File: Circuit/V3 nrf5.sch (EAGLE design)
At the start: 77 parts, among them J4 USB Micro, J7 CORTEX_DEBUG_SMD, Q1 BSS138, Q2 BSS84, U1 AL8805, U2 MCP73831, U3 BC840M, U4 3.3V/150mA, U5 AL8805, U6 AL8805, U8 TPS61235PRWLR, Y1 32.768kHz

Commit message: clean brd
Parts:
- D2: DIGIKEY 160-1837-1-ND -> (none)
- D9: DIGIKEY 160-1436-1-ND -> (none)
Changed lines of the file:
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@@
 <part name="GND1" library="SparkFun-PowerSymbols" deviceset="GND" device=""/>
 <part name="GND20" library="SparkFun-PowerSymbols" deviceset="GND" device=""/>
-<part name="D2" library="SparkFun-LED" library_urn="urn:adsk.eagle:library:529" deviceset="LED-BLUE" device="0603" package3d_urn="urn:adsk.eagle:package:39354/1" value="BLUE">
-<attribute name="DIGIKEY" value="160-1837-1-ND"/>
-</part>
 <part name="R5" library="SparkFun-Resistors" deviceset="1KOHM" device="-0603-1/10W-1%" value="1k">
 <attribute name="DIGIKEY" value="RMCF0603FG1K00"/>
@@
 <part name="D8" library="SparkFun-DiscreteSemi" deviceset="DIODE-SCHOTTKY" device="-B340A" value="3A/40V/500mV">
 <attribute name="DIGIKEY" value="B340A-E3/61TGICT-ND"/>
-</part>
-<part name="D9" library="SparkFun-LED" library_urn="urn:adsk.eagle:library:529" deviceset="LED-RED" device="0603" package3d_urn="urn:adsk.eagle:package:39354/1" value="RED">
-<attribute name="DIGIKEY" value="160-1436-1-ND"/>
 </part>
 <part name="C13" library="SparkFun-Capacitors" deviceset="22UF" device="-0805-6.3V-20%" value="22uF">
@@
 </part>
 <part name="GND38" library="SparkFun" deviceset="GND" device=""/>
+<part name="D2" library="SparkFun-LED" library_urn="urn:adsk.eagle:library:529" deviceset="LED-BLUE" device="0603" package3d_urn="urn:adsk.eagle:package:39354/1" value="BLUE"/>
+<part name="D9" library="SparkFun-LED" library_urn="urn:adsk.eagle:library:529" deviceset="LED-RED" device="0603" package3d_urn="urn:adsk.eagle:package:39354/1" value="RED"/>
 </parts>
 <sheets>
@@
 <attribute name="VALUE" x="416.56" y="136.906" size="1.778" layer="96" align="top-center"/>
 </instance>
-<instance part="D2" gate="G$1" x="360.68" y="157.48" smashed="yes" rot="R90">
-<attribute name="NAME" x="365.252" y="154.051" size="1.778" layer="95" font="vector" rot="R180"/>
-<attribute name="VALUE" x="365.252" y="159.385" size="1.778" layer="96" font="vector" rot="R180" align="top-left"/>
-<attribute name="DIGIKEY" x="360.68" y="157.48" size="3.4798" layer="96" ratio="10" rot="R90" display="off"/>
-</instance>
 <instance part="R5" gate="G$1" x="350.52" y="157.48" smashed="yes" rot="R180">
 <attribute name="NAME" x="350.52" y="155.956" size="1.778" layer="95" font="vector" rot="R180" align="bottom-center"/>
@@
 <attribute name="DIGIKEY" x="439.42" y="88.9" size="3.4798" layer="96" ratio="10" rot="R90" display="off"/>
 </instance>
-<instance part="D9" gate="G$1" x="414.02" y="78.74" smashed="yes">
-<attribute name="NAME" x="410.591" y="74.168" size="1.778" layer="95" font="vector" rot="R90"/>
-<attribute name="VALUE" x="415.925" y="74.168" size="1.778" layer="96" font="vector" rot="R90" align="top-left"/>
-<attribute name="DIGIKEY" x="414.02" y="78.74" size="3.4798" layer="96" ratio="10" display="off"/>
-</instance>
 <instance part="C13" gate="G$1" x="401.32" y="63.5" smashed="yes">
 <attribute name="NAME" x="402.844" y="66.421" size="1.778" layer="95" font="vector"/>
@@
 <instance part="GND38" gate="1" x="266.7" y="50.8" smashed="yes" rot="MR0">
 <attribute name="VALUE" x="269.24" y="48.26" size="1.778" layer="96" rot="MR0"/>
+</instance>
+<instance part="D2" gate="G$1" x="360.68" y="157.48" smashed="yes" rot="R90">
+<attribute name="NAME" x="365.252" y="154.051" size="1.778" layer="95" font="vector" rot="R180"/>
+<attribute name="VALUE" x="365.252" y="159.385" size="1.778" layer="96" font="vector" rot="R180" align="top-left"/>
+</instance>
+<instance part="D9" gate="G$1" x="414.02" y="78.74" smashed="yes">
+<attribute name="NAME" x="410.591" y="74.168" size="1.778" layer="95" font="vector" rot="R90"/>
+<attribute name="VALUE" x="415.925" y="74.168" size="1.778" layer="96" font="vector" rot="R90" align="top-left"/>
 </instance>
 </instances>
@@
 <pinref part="D7" gate="G$1" pin="C"/>
 <pinref part="D8" gate="G$1" pin="C"/>
-<pinref part="D9" gate="G$1" pin="A"/>
 <wire x1="414.02" y1="81.28" x2="414.02" y2="93.98" width="0.1524" layer="91"/>
 <pinref part="R7" gate="G$1" pin="2"/>
@@
 <wire x1="375.92" y1="93.98" x2="375.92" y2="86.36" width="0.1524" layer="91"/>
 <junction x="375.92" y="93.98"/>
+<pinref part="D9" gate="G$1" pin="A"/>
 </segment>
 <segment>
@@
 <net name="N$13" class="0">
 <segment>
-<pinref part="D9" gate="G$1" pin="C"/>
 <wire x1="414.02" y1="71.12" x2="414.02" y2="73.66" width="0.1524" layer="91"/>
 <pinref part="R14" gate="G$1" pin="1"/>
+<pinref part="D9" gate="G$1" pin="C"/>
 </segment>
 </net>
@@
 <segment>
 <pinref part="R5" gate="G$1" pin="1"/>
+<wire x1="355.6" y1="157.48" x2="358.14" y2="157.48" width="0.1524" layer="91"/>
 <pinref part="D2" gate="G$1" pin="A"/>
-<wire x1="355.6" y1="157.48" x2="358.14" y2="157.48" width="0.1524" layer="91"/>
-</segment>
-</net>
+</segment>
+</net>

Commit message: Rev 6 of the board is laid out and done, except for VDIV. Need to confirm what it's for and then send to the board house.
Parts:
- Q1: value BSS138 -> FDV301N; DIGIKEY BSS138CT-ND -> FDV301NCT-ND
- R13: value 332k -> 294k; DIGIKEY RMCF0603FT332K -> 311-294KHRCT-ND
- U8: value TPS61235PRWLR -> TPS61236P; DIGIKEY 296-47376-1-ND -> 296-44629-1-ND
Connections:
- net VBAT: no longer POWER_IN.+
- net VBAT_S: now also POWER_IN.+
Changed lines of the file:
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@@
 <drawing>
 <settings>
-<setting alwaysvectorfont="no"/>
+<setting alwaysvectorfont="yes"/>
 <setting keepoldvectorfont="yes"/>
 <setting verticaltext="up"/>
@@
 <attribute name="DIGIKEY" value="SAM1161-05-ND"/>
 </part>
-<part name="Q1" library="SparkFun" deviceset="MOSFET-NCHANNEL" device="SMD" value="BSS138">
-<attribute name="DIGIKEY" value="BSS138CT-ND"/>
+<part name="Q1" library="SparkFun" deviceset="MOSFET-NCHANNEL" device="SMD" value="FDV301N">
+<attribute name="DIGIKEY" value="FDV301NCT-ND"/>
 </part>
 <part name="R2" library="SparkFun" deviceset="RESISTOR" device="0603-RES" value="10K">
@@
 <attribute name="DIGIKEY" value="RMCF0603FT1M00"/>
 </part>
-<part name="R13" library="SparkFun-Resistors" deviceset="100KOHM" device="-0603-1/10W-1%" value="332k">
-<attribute name="DIGIKEY" value="RMCF0603FT332K"/>
+<part name="R13" library="SparkFun-Resistors" deviceset="100KOHM" device="-0603-1/10W-1%" value="294k">
+<attribute name="DIGIKEY" value="311-294KHRCT-ND"/>
 </part>
 <part name="GND22" library="SparkFun" deviceset="GND" device=""/>
@@
 <attribute name="DIGIKEY" value="563-1102-1-ND"/>
 </part>
-<part name="U8" library="TPS61235PRWLR" deviceset="TPS61235PRWLR" device="">
-<attribute name="DIGIKEY" value="296-47376-1-ND"/>
+<part name="U8" library="TPS61235PRWLR" deviceset="TPS61235PRWLR" device="" value="TPS61236P">
+<attribute name="DIGIKEY" value="296-44629-1-ND"/>
 </part>
 <part name="C1" library="SparkFun-Capacitors" deviceset="22UF" device="-0805-6.3V-20%" value="10uF">
@@
 <net name="VBAT" class="0">
 <segment>
-<pinref part="POWER_IN" gate="G$1" pin="+"/>
-<wire x1="-134.62" y1="25.4" x2="-124.46" y2="25.4" width="0.1524" layer="91"/>
-<label x="-124.46" y="25.4" size="1.778" layer="95" rot="R180"/>
-</segment>
-<segment>
 <pinref part="S3" gate="1" pin="O"/>
 <wire x1="213.36" y1="88.9" x2="215.9" y2="88.9" width="0.1524" layer="91"/>
@@
 <junction x="408.94" y="167.64"/>
 </segment>
-</net>
+<segment>
+<pinref part="POWER_IN" gate="G$1" pin="+"/>
+<wire x1="-134.62" y1="25.4" x2="-124.46" y2="25.4" width="0.1524" layer="91"/>
+<label x="-124.46" y="25.4" size="1.778" layer="95" rot="R180"/>
+</segment>
+</net>

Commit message: div clean
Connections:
- removed net VDIV: RN1C.2, RN1D.1, U3.A0/P101
- net GND: no longer RN1C.1
- net VBAT: no longer RN1D.2
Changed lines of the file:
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@@
 <drawing>
 <settings>
-<setting alwaysvectorfont="yes"/>
+<setting alwaysvectorfont="no"/>
 <setting keepoldvectorfont="yes"/>
 <setting verticaltext="up"/>
@@
 </part>
 <part name="GND6" library="SparkFun" deviceset="GND" device=""/>
-<part name="GND14" library="SparkFun" deviceset="GND" device=""/>
 <part name="S2" library="SparkFun-Switches" library_urn="urn:adsk.eagle:library:535" deviceset="MOMENTARY-SWITCH-SPST-2" device="-SMD-4.6X2.8MM" package3d_urn="urn:adsk.eagle:package:40176/1">
 <attribute name="DIGIKEY" value="401-1426-1-ND"/>
@@
 <attribute name="NAME" x="376.428" y="15.24" size="1.778" layer="95" rot="R90"/>
 </instance>
-<instance part="RN1" gate="C" x="238.76" y="15.24" smashed="yes" rot="R90">
-<attribute name="VALUE" x="241.808" y="17.78" size="1.778" layer="96" rot="R90"/>
-<attribute name="NAME" x="241.808" y="10.16" size="1.778" layer="95" rot="R90"/>
-</instance>
-<instance part="RN1" gate="D" x="238.76" y="33.02" smashed="yes" rot="R90">
-<attribute name="VALUE" x="241.808" y="35.56" size="1.778" layer="96" rot="R90"/>
-<attribute name="NAME" x="241.808" y="27.94" size="1.778" layer="95" rot="R90"/>
-</instance>
 <instance part="D10" gate="G$1" x="347.98" y="27.94" smashed="yes">
 <attribute name="NAME" x="350.52" y="28.4226" size="1.778" layer="95"/>
@@
 <instance part="GND6" gate="1" x="386.08" y="7.62" smashed="yes">
 <attribute name="VALUE" x="383.54" y="5.08" size="1.778" layer="96"/>
-</instance>
-<instance part="GND14" gate="1" x="238.76" y="5.08" smashed="yes" rot="MR0">
-<attribute name="VALUE" x="241.3" y="2.54" size="1.778" layer="96" rot="MR0"/>
 </instance>
 <instance part="S2" gate="G$1" x="22.86" y="33.02" smashed="yes">
@@
 <pinref part="GND6" gate="1" pin="GND"/>
 <wire x1="386.08" y1="17.78" x2="386.08" y2="10.16" width="0.1524" layer="91"/>
-</segment>
-<segment>
-<pinref part="RN1" gate="C" pin="1"/>
-<wire x1="238.76" y1="10.16" x2="238.76" y2="7.62" width="0.1524" layer="91"/>
-<pinref part="GND14" gate="1" pin="GND"/>
 </segment>
 <segment>
@@
 <wire x1="129.54" y1="45.72" x2="129.54" y2="48.26" width="0.1524" layer="91"/>
 <wire x1="129.54" y1="48.26" x2="129.54" y2="50.8" width="0.1524" layer="91"/>
-<wire x1="137.16" y1="40.64" x2="137.16" y2="48.26" width="0.1524" layer="91"/>
 <wire x1="137.16" y1="48.26" x2="129.54" y2="48.26" width="0.1524" layer="91"/>
 <junction x="129.54" y="48.26"/>
 <pinref part="R2" gate="G$1" pin="1"/>
+<pinref part="P+15" gate="G$1" pin="3.3V"/>
+<wire x1="137.16" y1="48.26" x2="137.16" y2="43.18" width="0.1524" layer="91"/>
 <pinref part="Q1" gate="G$1" pin="G"/>
-<pinref part="P+15" gate="G$1" pin="3.3V"/>
+<wire x1="137.16" y1="43.18" x2="137.16" y2="41.91" width="0.1524" layer="91"/>
+<wire x1="137.16" y1="40.64" x2="137.16" y2="41.91" width="0.1524" layer="91"/>
 </segment>
 <segment>
@@
 <pinref part="U4" gate="U1" pin="EN"/>
 <wire x1="378.46" y1="22.86" x2="388.62" y2="22.86" width="0.1524" layer="91"/>
-</segment>
-</net>
-<net name="VDIV" class="0">
-<segment>
-<pinref part="RN1" gate="C" pin="2"/>
-<pinref part="RN1" gate="D" pin="1"/>
-<wire x1="238.76" y1="20.32" x2="238.76" y2="25.4" width="0.1524" layer="91"/>
-<wire x1="238.76" y1="25.4" x2="238.76" y2="27.94" width="0.1524" layer="91"/>
-<wire x1="238.76" y1="25.4" x2="248.92" y2="25.4" width="0.1524" layer="91"/>
-<junction x="238.76" y="25.4"/>
-<label x="248.92" y="25.4" size="1.778" layer="95"/>
-</segment>
-<segment>
-<pinref part="U3" gate="G$1" pin="A0/P101"/>
-<wire x1="53.726" y1="163.534" x2="38.354" y2="163.534" width="0.1524" layer="91"/>
-<wire x1="38.354" y1="163.534" x2="38.354" y2="163.576" width="0.1524" layer="91"/>
-<label x="38.1" y="164.084" size="1.778" layer="95"/>
 </segment>
 </net>
@@
 </segment>
 <segment>
-<pinref part="RN1" gate="D" pin="2"/>
-<wire x1="238.76" y1="38.1" x2="238.76" y2="43.18" width="0.1524" layer="91"/>
-<label x="238.76" y="43.18" size="1.016" layer="95" xref="yes"/>
-</segment>
-<segment>

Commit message: Adding digikey parts, updating bom for rev6.
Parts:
- D2: DIGIKEY (none) -> 160-1647-1-ND
- D9: DIGIKEY (none) -> 160-1436-1-ND
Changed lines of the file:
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@@
 <drawing>
 <settings>
-<setting alwaysvectorfont="no"/>
+<setting alwaysvectorfont="yes"/>
 <setting keepoldvectorfont="yes"/>
 <setting verticaltext="up"/>
@@
 </part>
 <part name="GND38" library="SparkFun" deviceset="GND" device=""/>
-<part name="D2" library="SparkFun-LED" library_urn="urn:adsk.eagle:library:529" deviceset="LED-BLUE" device="0603" package3d_urn="urn:adsk.eagle:package:39354/1" value="BLUE"/>
-<part name="D9" library="SparkFun-LED" library_urn="urn:adsk.eagle:library:529" deviceset="LED-RED" device="0603" package3d_urn="urn:adsk.eagle:package:39354/1" value="RED"/>
+<part name="D2" library="SparkFun-LED" library_urn="urn:adsk.eagle:library:529" deviceset="LED-BLUE" device="0603" package3d_urn="urn:adsk.eagle:package:39354/1" value="BLUE">
+<attribute name="DIGIKEY" value="160-1647-1-ND"/>
+</part>
+<part name="D9" library="SparkFun-LED" library_urn="urn:adsk.eagle:library:529" deviceset="LED-RED" device="0603" package3d_urn="urn:adsk.eagle:package:39354/1" value="RED">
+<attribute name="DIGIKEY" value="160-1436-1-ND"/>
+</part>
 </parts>
 <sheets>
@@
 <attribute name="NAME" x="269.228109375" y="165.633" size="1.782159375" layer="95"/>
 <attribute name="VALUE" x="269.22208125" y="142.1952" size="1.78428125" layer="96"/>
-<attribute name="DIGIKEY" x="274.32" y="154.94" size="3.4798" layer="96" ratio="10" display="off"/>
+<attribute name="DIGIKEY" x="274.32" y="154.94" size="1.778" layer="96" display="off"/>
 </instance>
 <instance part="S3" gate="1" x="208.28" y="86.36" smashed="yes">
@@
 <attribute name="NAME" x="365.252" y="154.051" size="1.778" layer="95" font="vector" rot="R180"/>
 <attribute name="VALUE" x="365.252" y="159.385" size="1.778" layer="96" font="vector" rot="R180" align="top-left"/>
+<attribute name="DIGIKEY" x="360.68" y="157.48" size="1.778" layer="96" rot="R90" display="off"/>
 </instance>
 <instance part="D9" gate="G$1" x="414.02" y="78.74" smashed="yes">
 <attribute name="NAME" x="410.591" y="74.168" size="1.778" layer="95" font="vector" rot="R90"/>
 <attribute name="VALUE" x="415.925" y="74.168" size="1.778" layer="96" font="vector" rot="R90" align="top-left"/>
+<attribute name="DIGIKEY" x="414.02" y="78.74" size="1.778" layer="96" display="off"/>
 </instance>
 </instances>

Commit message: Updating digikey parts.
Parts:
- R10: DIGIKEY A130088CT-ND -> P330HCT-ND
- R15: DIGIKEY P10KGCT-ND -> A103067TR-ND
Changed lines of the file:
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@@
 </part>
 <part name="R10" library="SparkFun" deviceset="RESISTOR" device="0603-RES" value="330">
-<attribute name="DIGIKEY" value="A130088CT-ND"/>
+<attribute name="DIGIKEY" value="P330HCT-ND"/>
 </part>
 <part name="GND18" library="SparkFun" deviceset="GND" device=""/>
@@
 </part>
 <part name="R15" library="SparkFun" deviceset="RESISTOR" device="0603-RES" value="22">
-<attribute name="DIGIKEY" value="P10KGCT-ND"/>
+<attribute name="DIGIKEY" value="A103067TR-ND "/>
 </part>
 <part name="C18" library="SparkFun-Capacitors" deviceset="4.7UF" device="0603" value="4.7uF">

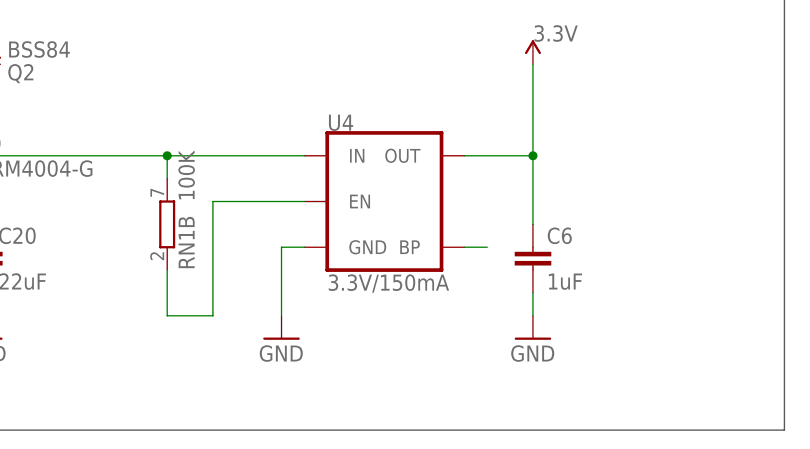
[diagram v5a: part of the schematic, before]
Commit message: Changing pins to match board.
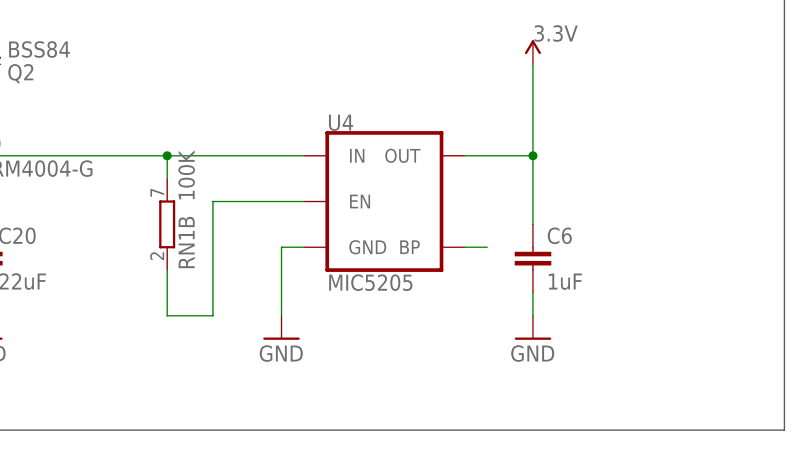
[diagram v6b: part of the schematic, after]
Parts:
- U4: value 3.3V/150mA -> MIC5205
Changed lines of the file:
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@@
 <attribute name="DIGIKEY" value="MBR120VLSFT1G"/>
 </part>
-<part name="U4" library="SparkFun-IC-Power" library_urn="urn:adsk.eagle:library:526" deviceset="V_REG_MIC5205" device="3.3V" package3d_urn="urn:adsk.eagle:package:39060/1" value="3.3V/150mA">
+<part name="U4" library="SparkFun-IC-Power" library_urn="urn:adsk.eagle:library:526" deviceset="V_REG_MIC5205" device="3.3V" package3d_urn="urn:adsk.eagle:package:39060/1" value="MIC5205">
 <attribute name="DIGIKEY" value="576-1259-1-ND"/>
 </part>

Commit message: Removing picobuck, touching up and finalizing schematic layout, switching to neopixel 3W led (headlamp). Needs new dimensions to fit with battery in enclosure.
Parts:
- removed C14, C4, C8: 2.2uF, SparkFun-Capacitors:2.2UF50V10%(1206)
- removed C2, C5, C7: 1uF, SparkFun-Capacitors:1.0UF50V10%(1206)
- removed D4, D5, D6: 3A/40V/500mV, SparkFun-DiscreteSemi:DIODE-SCHOTTKY-B340A
- removed J2, J3: (no value), SparkFun-Connectors:CONN_023.5MM
- removed JP3: JUMPER-SMT_3_1-NC, SparkFun-Jumpers:JUMPER-SMT_3_1-NC_PASTE_NO-SILK
- removed L1, L2, L3: 33uH, SparkFun-Passives:INDUCTORBOURNS_SRN6045
- removed R12, R2: 10K, SparkFun:RESISTOR0603-RES
- removed R3, R9: 0.3R, SparkFun-Resistors:0.3OHM-1/8W-1%(0805)
- removed U1, U5, U6: AL8805, SparkFun-PowerIC:AL8805
- added Q3: FDV301N, SparkFun:MOSFET-NCHANNELSMD
- added RN2: (no value), resistor-dil:4R-NEXBV8V
- added TP5: TPSB1,27, testpad:TPSB1,27
- C1, C11: value 10uF -> 22uF
- C16, C6: value 1uF -> 22uF
- J1: device SparkFun-Connectors:CONN_023.5MM -> SparkFun-Connectors:CONN_03SCREW_LOCK; DIGIKEY 277-1721-ND -> (none)
- R1: value 0.3R -> 330; device SparkFun-Resistors:0.3OHM-1/8W-1%(0805) -> SparkFun:RESISTOR0603-RES; DIGIKEY A138521CT-ND -> P330HCT-ND
- R13: value 294k -> 100k
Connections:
- removed net OUT1+: C7.1, J1.2, R1.2, U1.SET
- removed net OUT1-: C7.2, J1.1, L1.2
- removed net OUT2+: C2.1, J2.2, R3.2, U5.SET
- removed net OUT2-: C2.2, J2.1, L2.2
- removed net OUT3+: C5.1, J3.2, R9.2, U6.SET
- removed net OUT3-: C5.2, J3.1, L3.2
- removed net SW: D4.A, L1.1, U1.SW
- removed net SW1: D5.A, L2.1, U5.SW
- removed net SW2: D6.A, L3.1, U6.SW
- new net HEADLAMP_3V3: Q3.S, RN2B.1, TP5.PP, U3.G1/P030
- new net HEADLAMP_5V: Q3.D, R1.2, RN2D.1
- new net N$17: J1.2, R1.1
- net 3.3V: now also Q3.G, RN2A.2, RN2B.2; no longer JP3.3, R2.1
- net 5V: now also J1.3, RN2C.2, RN2D.2; no longer C14.1, C4.1, C8.1, D4.C, D5.C, D6.C, R1.1, R12.1, R3.1, R9.1, U1.VIN, U5.VIN, U6.VIN
- net CTRL_CH1: no longer U1.CTRL
- net CTRL_CH2: no longer U5.CTRL
- net CTRL_CH3: no longer U6.CTRL
- net GND: now also J1.1; no longer C14.2, C4.2, C8.2, U1.GND, U5.GND, U6.GND
- net STRIP_3V3: now also RN2A.1; no longer R2.2
- net STRIP_5V: now also RN2C.1; no longer R12.2
- net VBAT_S: no longer JP3.1
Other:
- note added: "Input is 5V from nrf52 Output is to 3V3 leds"
- note added: "Level shifter"
- note added: "debug led"
- note added: "headlamp"
- note added: "nrf52840 radio"
- note added: "reset button"
- note added: "status led"
- note added: "swd programmer"
- note added: "user button"
- note removed: "6V < VIN < 36V"
- note removed: "I_LED = 0.1 / R1 = 350mA"
- note removed: "LED DRIVERS"
- note removed: "Led driver for dynamically controlling the current"
- moved on the sheet: C1, C11, C13, C15, C16, C17, C19, C20, C3, C6, C9, D1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

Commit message: Finishing V7 of the board. All connectors are on two sides of the board now, making the enclosure more seamless. Off to the board house!
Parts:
- J1: DIGIKEY (none) -> A98037-ND
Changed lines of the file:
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@@
 <attribute name="DIGIKEY" value="YC164-JR-0710KL"/>
 </part>
-<part name="J1" library="SparkFun-Connectors" library_urn="urn:adsk.eagle:library:513" deviceset="CONN_03" device="SCREW_LOCK" package3d_urn="urn:adsk.eagle:package:38066/1"/>
+<part name="J1" library="SparkFun-Connectors" library_urn="urn:adsk.eagle:library:513" deviceset="CONN_03" device="SCREW_LOCK" package3d_urn="urn:adsk.eagle:package:38066/1">
+<attribute name="DIGIKEY" value="A98037-ND"/>
+</part>
 <part name="GND4" library="SparkFun" deviceset="GND" device=""/>
 <part name="R1" library="SparkFun" deviceset="RESISTOR" device="0603-RES" value="330">
@@
 <attribute name="VALUE" x="-63.5" y="109.474" size="1.778" layer="96" font="vector"/>
 <attribute name="NAME" x="-63.5" y="122.428" size="1.778" layer="95" font="vector"/>
+<attribute name="DIGIKEY" x="-60.96" y="116.84" size="3.302" layer="96" display="off"/>
 </instance>
 <instance part="GND4" gate="1" x="-45.72" y="104.14" smashed="yes" rot="MR0">
